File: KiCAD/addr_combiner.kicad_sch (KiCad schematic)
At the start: 0 parts

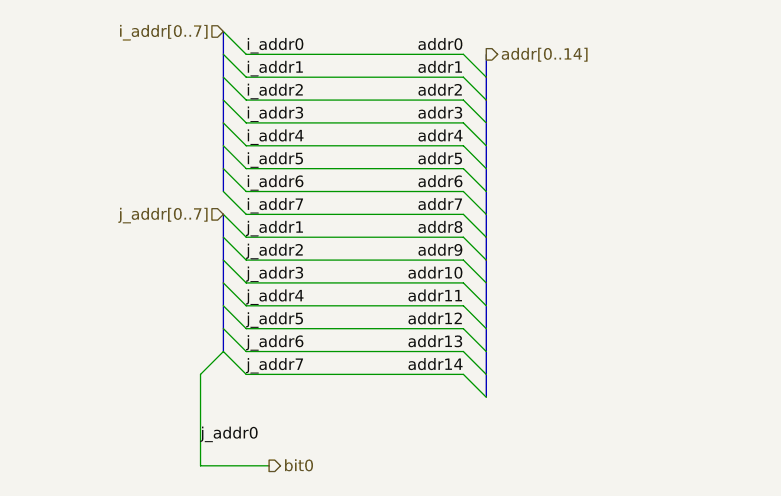
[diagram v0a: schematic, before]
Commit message: fix multiple ERCs that made RAM addrs not connecting
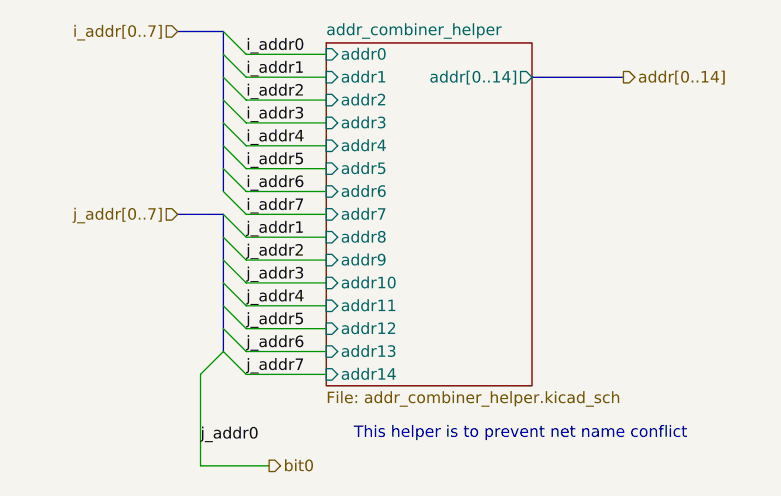
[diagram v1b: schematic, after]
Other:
- added sheet addr_combiner_helper (addr_combiner_helper.kicad_sch)
- note added: "This helper is to prevent net name conflict"

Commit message: resolved most ERC errors
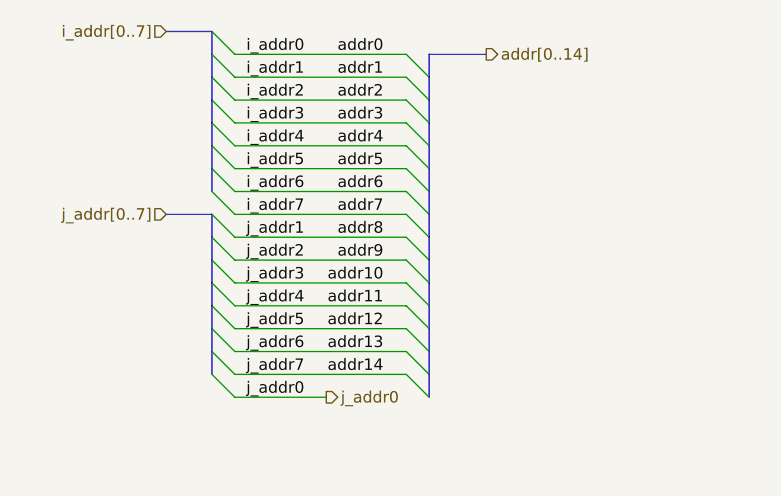
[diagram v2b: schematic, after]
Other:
- removed sheet addr_combiner_helper
- note removed: "This helper is to prevent net name conflict"

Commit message: resolved all ERC errors, kicad got some stupid bugs
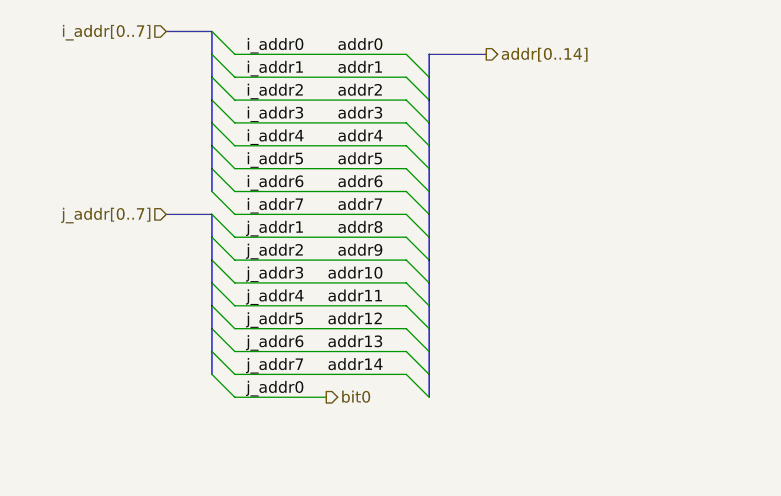
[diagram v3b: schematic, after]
